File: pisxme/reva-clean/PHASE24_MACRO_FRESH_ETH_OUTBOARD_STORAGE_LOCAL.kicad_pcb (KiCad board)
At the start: 6 copper layers, 300 x 180 mm, 101 parts, among them J1 74221-101LF, J2 A70-112-331N126, J3 JAE SM3ZS067U410ABR1000 B-key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, J4 Amphenol 10171746-00021LF USB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, J5 0039300020, J6 0039300020, J7 Raspberry-Pi-5-Compute-Module, Q1 CSD19536KCS, Q2 CSD19536KCS, U1 LM74700QDBVRQ1, U2 LM74700QDBVRQ1, U3 TPSM63606RDLR, U4 TPSM63606RDLR, U5 TPSM63606RDLR, U6 TPD4EUSB30, U7 TUSB9261IPVP, U8 Texas_DRT_3, U9 TPD4EUSB30

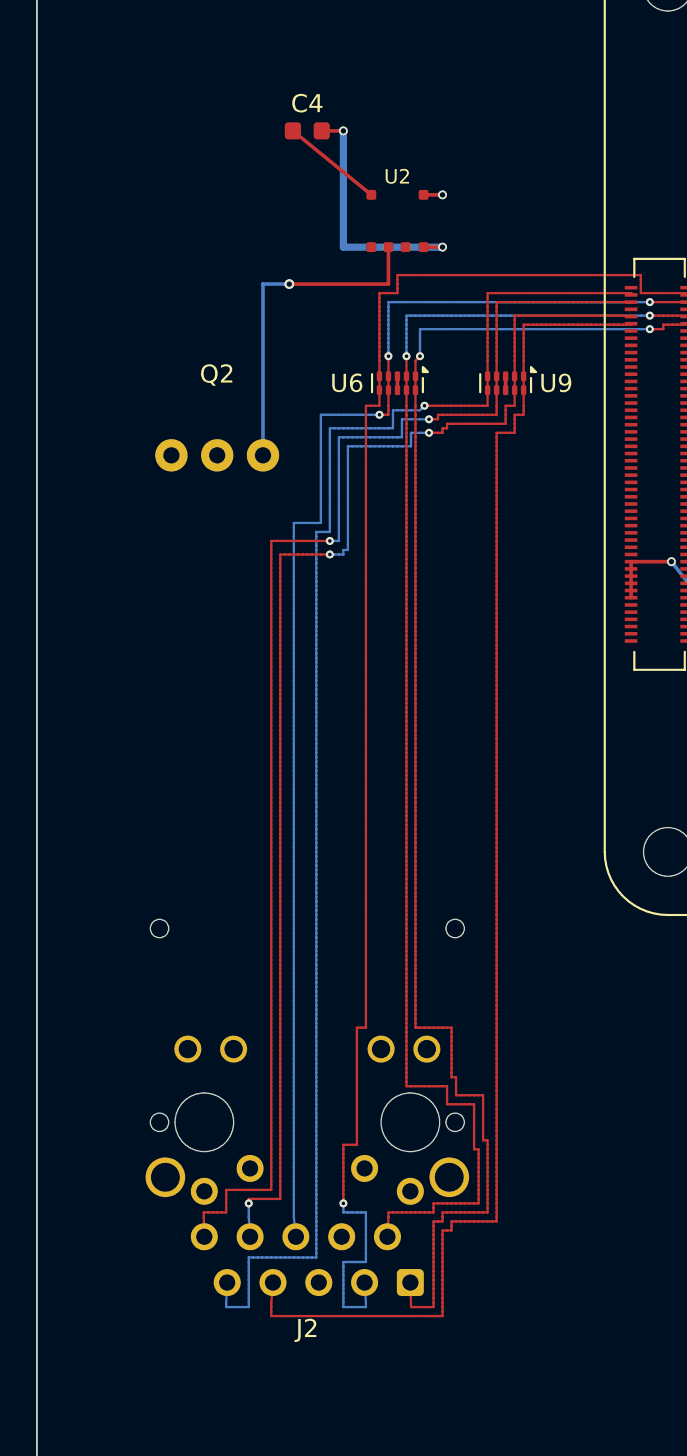
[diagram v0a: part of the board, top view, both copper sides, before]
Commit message: phase24: complete current-basis macro floorplan discriminator
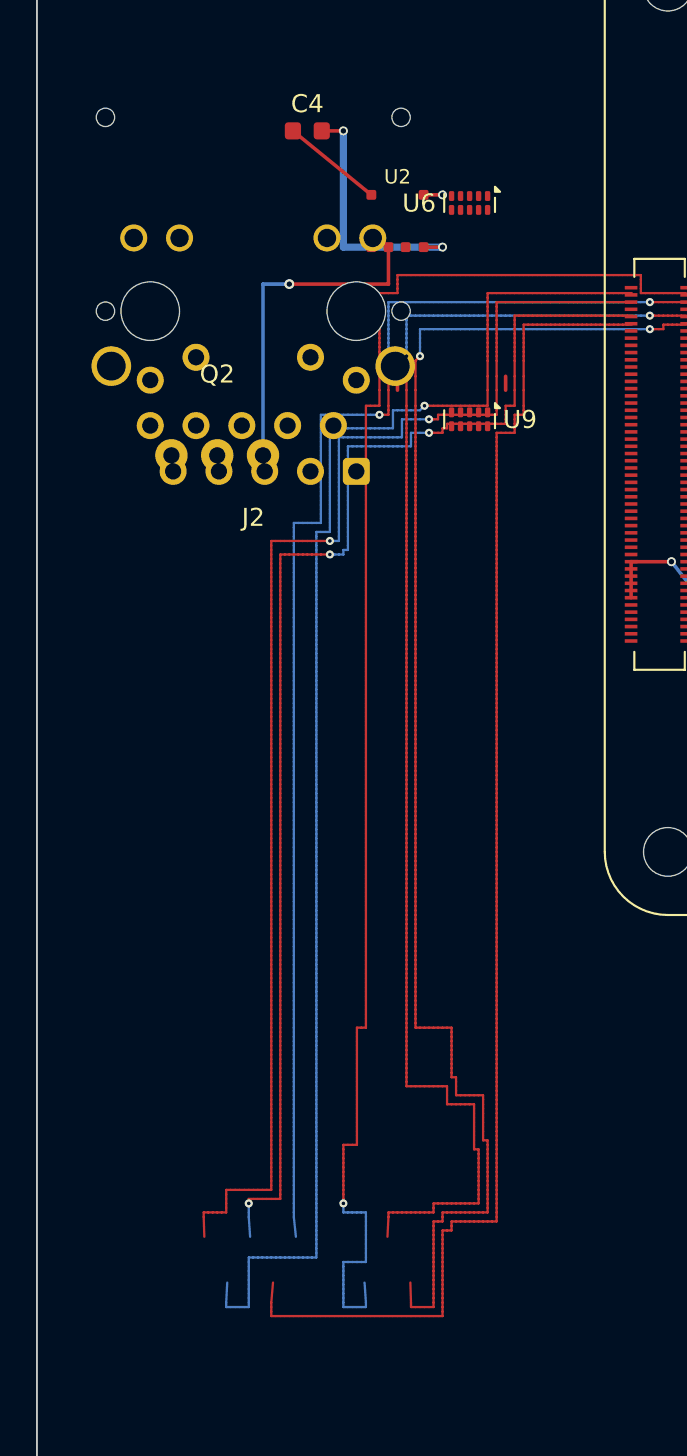
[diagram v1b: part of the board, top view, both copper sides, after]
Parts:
- moved J2 45.1 mm to (12.0, 100.0)
- moved U6 10.8 mm to (24.0, 94.0)
- moved U9 2.83 mm to (24.0, 106.0)
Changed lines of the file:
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@@
 	(footprint "Package_SON:USON-10_2.5x1.0mm_P0.5mm"
 		(layer "F.Cu")
-		(at 26 104 -90)
+		(at 24 106 -90)
 		(descr "USON-10 2.5x1.0mm_ Pitch 0.5mm http://www.ti.com/lit/ds/symlink/tpd4e02b04.pdf")
 		(tags "USON-10 2.5x1.0mm Pitch 0.5mm")
@@
 	(footprint "Package_SON:USON-10_2.5x1.0mm_P0.5mm"
 		(layer "F.Cu")
-		(at 20 104 -90)
+		(at 24 94 -90)
 		(descr "USON-10 2.5x1.0mm_ Pitch 0.5mm http://www.ti.com/lit/ds/symlink/tpd4e02b04.pdf")
 		(tags "USON-10 2.5x1.0mm Pitch 0.5mm")
@@
 	(footprint "EDAC_A70_112_331N126"
 		(layer "F.Cu")
-		(at 15 145 180)
+		(at 12 100 180)
 		(descr "EDAC A70-112-331N126; EDAC drawing via Mouser; no 3D model attached")
 		(tags "RJ45 MagJack Ethernet PoE EDAC A70-112-331N126")
